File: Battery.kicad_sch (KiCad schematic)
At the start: 12 parts, among them J1 Keystone-1048, J2 Keystone-1048, J3 Keystone-1042, J4 Keystone-1042

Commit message: temporary changes
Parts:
- added D7, D8: BAT60JFILM, Diode_SMD:D_SOD-323_HandSoldering, symbol Device:D_Schottky_Small
- added F12, F13, F14, F15: 5A, Fuse:Fuse_1206_3216Metric, symbol Device:Fuse_Small
- added J11: (no value), Argus-Battery:21700_battery_holder_th, symbol Argus-Battery:21700_batt_holder_th
- D1, D2, F1, F2, F3, F4, F5, F6, J1, J2, J3, J4: now not fitted
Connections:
- net BATT_M: now also D7.1 (K), D8.2 (A), J11.5 (neg1), J11.6 (neg2), J11.7 (pos3), J11.8 (pos4)
- net BATT_N: now also D7.2 (A), F12.2, F13.2
- net BATT_P: now also D8.1 (K), F14.2, F15.2
- new net: F15.1, J11.2 (pos2)
- new net: F13.1, J11.3 (neg3)
- new net: F12.1, J11.4 (neg4)
- new net: F14.1, J11.1 (pos1)
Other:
- note added: "4x 21700 cells in 2s2p configuration 7.2V nominal, 10000mAh Capacity Molicel 21700 P50B 5000mAh 60A Battery"

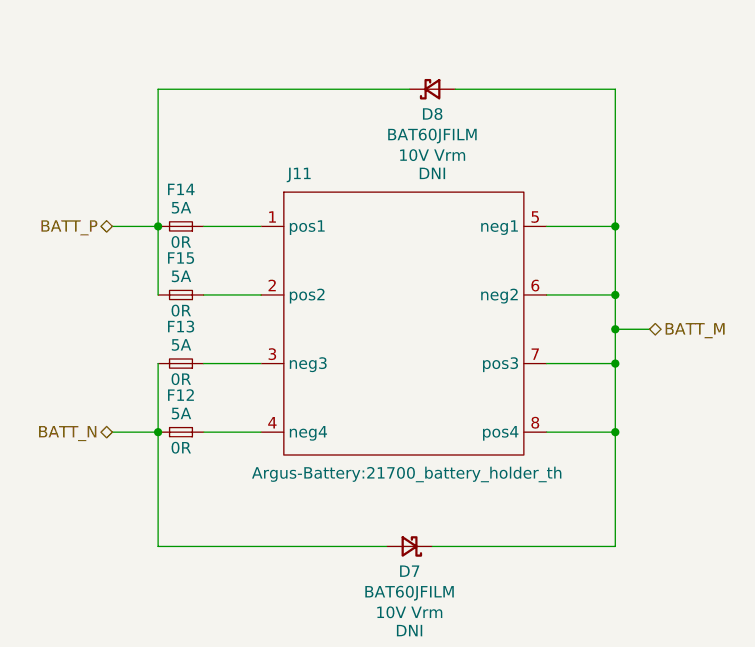
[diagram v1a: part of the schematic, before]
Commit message: placed components start routing
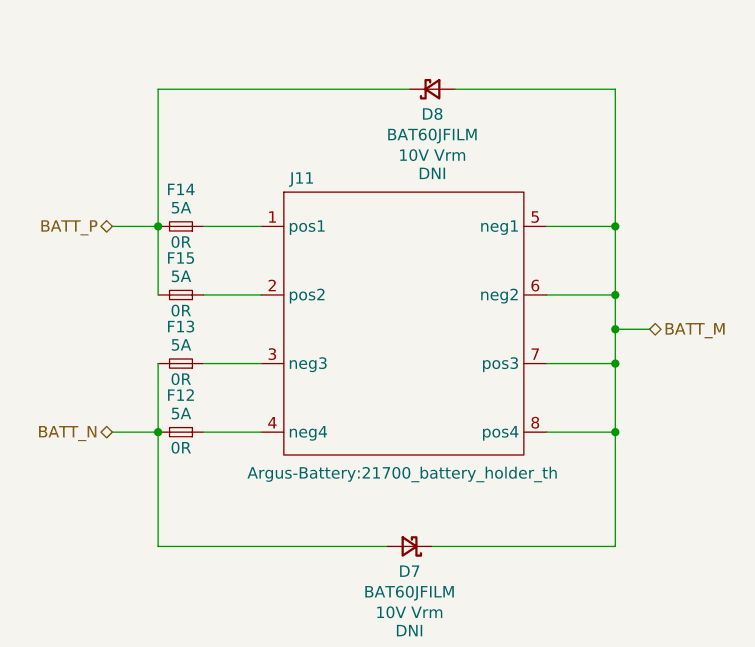
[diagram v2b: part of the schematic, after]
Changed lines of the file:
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@@
+	)
+	(symbol
+		(lib_id "Argus-Battery:21700_batt_holder_th")
+		(at 205.74 64.77 0)
+		(unit 1)
+		(body_style 1)
+		(exclude_from_sim no)
+		(in_bom no)
+		(on_board yes)
+		(in_pos_files no)
+		(dnp no)
+		(property "Reference" "J11"
+			(at 211.582 64.516 0)
+			(show_name no)
+			(do_not_autoplace no)
+			(effects
+				(font
+					(size 1.27 1.27)
+				)
+			)
+		)
+		(property "Value" ""
+			(at 205.74 64.77 0)
+			(show_name no)
+			(do_not_autoplace no)
+			(effects
+				(font
+					(size 1.27 1.27)
+				)
+			)
+		)
+		(property "Footprint" "Argus-Battery:21700_battery_holder_th"
+			(at 222.758 97.282 0)
+			(show_name no)
+			(do_not_autoplace no)
+			(effects
+				(font
+					(size 1.27 1.27)
+				)
+			)
+		)
+		(property "Datasheet" ""
+			(at 205.74 64.77 0)
+			(hide yes)
+			(show_name no)
+			(do_not_autoplace no)
+			(effects
+				(font
+					(size 1.27 1.27)
+				)
+			)
+		)
+		(property "Description" ""
+			(at 205.74 64.77 0)
+			(hide yes)
+			(show_name no)
+			(do_not_autoplace no)
+			(effects
+				(font
+					(size 1.27 1.27)
+				)
+			)
+		)
+		(pin "3"
+		)
+		(pin "1"
+		)
+		(pin "5"
+		)
+		(pin "7"
+		)
+		(pin "6"
+		)
+		(pin "8"
+		)
+		(pin "2"
+		)
+		(pin "4"
+		)
+		(instances
+			(project "Avionics-BatteryBoard"
+				(path "/b6fd875d-6e05-4440-9a05-0f0aa046a0ef/929ad239-5e24-4db1-ba18-c148cf561726"
+					(reference "J11")
+					(unit 1)
+				)
+			)
+		)
 	)
 	(symbol
@@
 					(unit 1)
 				)
-			)
-		)
-	)
-	(symbol
-		(lib_id "Argus-Battery:21700_batt_holder_th")
-		(at 205.74 64.77 0)
-		(unit 1)
-		(body_style 1)
-		(exclude_from_sim no)
-		(in_bom no)
-		(on_board yes)
-		(in_pos_files no)
-		(dnp no)
-		(property "Reference" "J11"
-			(at 211.328 64.008 0)
-			(show_name no)
-			(do_not_autoplace no)
-			(effects
-				(font
-					(size 1.27 1.27)
-				)
-			)
-		)
-		(property "Value" ""
-			(at 205.74 64.77 0)
-			(show_name no)
-			(do_not_autoplace no)
-			(effects
-				(font
-					(size 1.27 1.27)
-				)
-			)
-		)
-		(property "Footprint" "Argus-Battery:21700_battery_holder_th"
-			(at 223.266 97.282 0)
-			(show_name no)
-			(do_not_autoplace no)
-			(effects
-				(font
-					(size 1.27 1.27)
-				)
-			)
-		)
-		(property "Datasheet" ""
-			(at 205.74 64.77 0)
-			(hide yes)
-			(show_name no)
-			(do_not_autoplace no)
-			(effects
-				(font
-					(size 1.27 1.27)
-				)
-			)
-		)
-		(property "Description" ""
-			(at 205.74 64.77 0)
-			(hide yes)
-			(show_name no)
-			(do_not_autoplace no)
-			(effects
-				(font
-					(size 1.27 1.27)
-				)
-			)
-		)
-		(pin "4"
-		)
-		(pin "5"
-		)
-		(pin "6"
-		)
-		(pin "1"
-		)
-		(pin "2"
-		)
-		(pin "3"
-		)
-		(pin "8"
-		)
-		(pin "7"
-		)
-		(instances
-			(project "Avionics-BatteryBoard"
-				(path "/b6fd875d-6e05-4440-9a05-0f0aa046a0ef/929ad239-5e24-4db1-ba18-c148cf561726"
-					(reference "J11")
-					(unit 1)
-				)

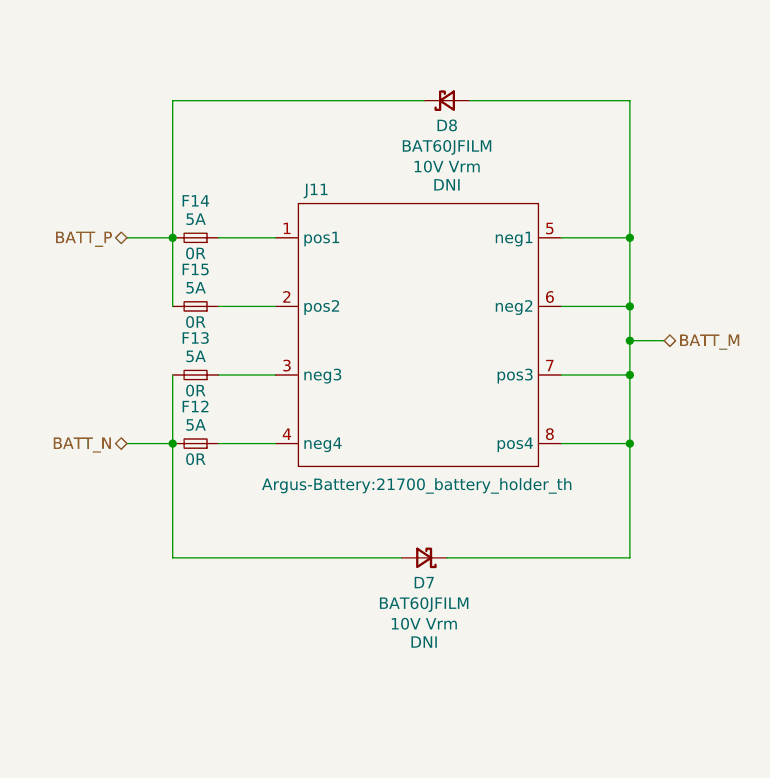
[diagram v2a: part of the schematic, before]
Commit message: batteryboard v4.0 complete, need to fix footprint courtyard so drc passes but othw should be all good
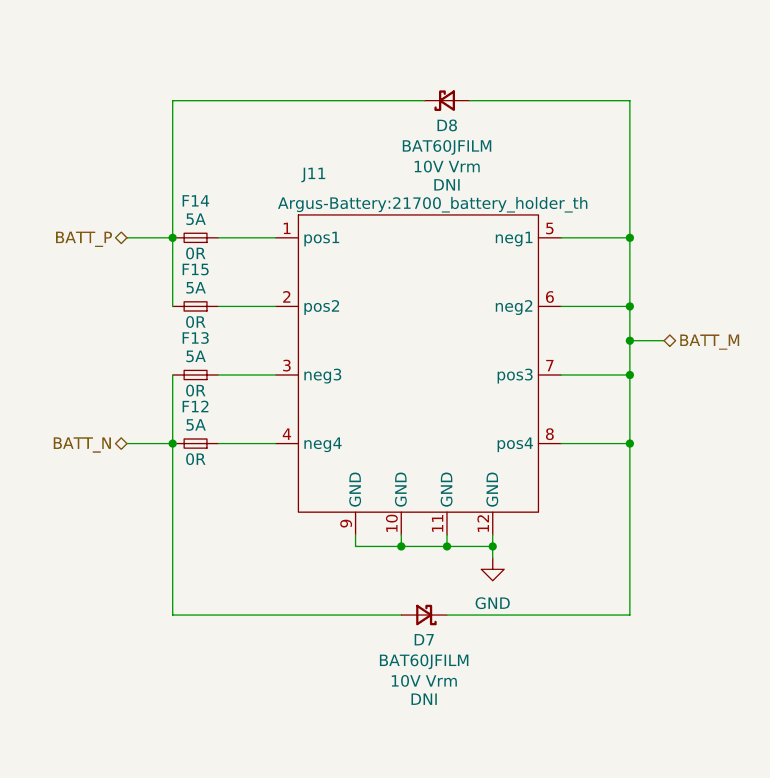
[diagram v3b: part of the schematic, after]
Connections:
- new net GND: J11.10 (GND), J11.11 (GND), J11.12 (GND), J11.9 (GND)
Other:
- moved on the sheet: D7
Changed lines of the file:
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@@
+	)
+	(junction
+		(at 246.38 92.71)
+		(diameter 0)
+		(color 0 0 0 0)
 	)
 	(junction
@@
 	)
 	(junction
+		(at 231.14 104.14)
+		(diameter 0)
+		(color 0 0 0 0)
+	)
+	(junction
 		(at 246.38 69.85)
 		(diameter 0)
@@
 	)
 	(junction
-		(at 246.38 92.71)
+		(at 226.06 104.14)
 		(diameter 0)
 		(color 0 0 0 0)
@@
 	)
 	(junction
+		(at 220.98 104.14)
+		(diameter 0)
+		(color 0 0 0 0)
+	)
+	(junction
 		(at 111.76 101.6)
 		(diameter 0)
@@
 	(wire
 		(pts
+			(xy 215.9 104.14) (xy 220.98 104.14)
+		)
+		(stroke
+			(width 0)
+			(type default)
+		)
+	)
+	(wire
+		(pts
 			(xy 76.2 101.6) (xy 76.2 113.03)
 		)
@@
 	(wire
 		(pts
+			(xy 226.06 104.14) (xy 226.06 102.87)
+		)
+		(stroke
+			(width 0)
+			(type default)
+		)
+	)
+	(wire
+		(pts
 			(xy 200.66 77.47) (xy 207.01 77.47)
 		)
@@
 	(wire
 		(pts
+			(xy 226.06 104.14) (xy 231.14 104.14)
+		)
+		(stroke
+			(width 0)
+			(type default)
+		)
+	)
+	(wire
+		(pts
 			(xy 40.64 90.17) (xy 40.64 101.6)
 		)
@@
 	(wire
 		(pts
+			(xy 220.98 104.14) (xy 220.98 102.87)
+		)
+		(stroke
+			(width 0)
+			(type default)
+		)
+	)
+	(wire
+		(pts
 			(xy 111.76 90.17) (xy 111.76 101.6)
 		)
@@
 	(wire
 		(pts
+			(xy 215.9 104.14) (xy 215.9 102.87)
+		)
+		(stroke
+			(width 0)
+			(type default)
+		)
+	)
+	(wire
+		(pts
 			(xy 107.95 101.6) (xy 111.76 101.6)
 		)
@@
 	(wire
 		(pts
-			(xy 226.06 105.41) (xy 246.38 105.41)
+			(xy 226.06 111.76) (xy 246.38 111.76)
 		)
 		(stroke
@@
 	(wire
 		(pts
+			(xy 220.98 104.14) (xy 226.06 104.14)
+		)
+		(stroke
+			(width 0)
+			(type default)
+		)
+	)
+	(wire
+		(pts
+			(xy 231.14 105.41) (xy 231.14 104.14)
+		)
+		(stroke
+			(width 0)
+			(type default)
+		)
+	)
+	(wire
+		(pts
 			(xy 195.58 54.61) (xy 195.58 69.85)
 		)
@@
 	(wire
 		(pts
-			(xy 246.38 105.41) (xy 246.38 92.71)
+			(xy 231.14 102.87) (xy 231.14 104.14)
+		)
+		(stroke
+			(width 0)
+			(type default)
+		)
+	)
+	(wire
+		(pts
+			(xy 246.38 111.76) (xy 246.38 92.71)
 		)
 		(stroke
@@
 	(wire
 		(pts
-			(xy 195.58 92.71) (xy 195.58 105.41)
+			(xy 195.58 92.71) (xy 195.58 111.76)
 		)
 		(stroke
@@
 	(wire
 		(pts
-			(xy 195.58 105.41) (xy 220.98 105.41)
+			(xy 195.58 111.76) (xy 220.98 111.76)
 		)
 		(stroke
@@
 	(symbol
 		(lib_id "Device:D_Schottky_Small")
-		(at 223.52 105.41 180)
+		(at 223.52 111.76 180)
 		(unit 1)
 		(body_style 1)
@@
 		(dnp no)
 		(property "Reference" "D7"
-			(at 223.52 108.204 0)
+			(at 223.52 114.554 0)
 			(show_name no)
 			(do_not_autoplace no)
@@
 		)
 		(property "Value" "BAT60JFILM"
-			(at 223.52 110.49 0)
+			(at 223.52 116.84 0)
 			(show_name no)
 			(do_not_autoplace no)
@@
 		)
 		(property "Footprint" "Diode_SMD:D_SOD-323_HandSoldering"
-			(at 223.52 105.41 90)
+			(at 223.52 111.76 90)
 			(hide yes)
 			(show_name no)
@@
 		)
 		(property "Datasheet" ""
-			(at 223.52 105.41 90)
+			(at 223.52 111.76 90)
 			(hide yes)
 			(show_name no)
@@
 		)
 		(property "Description" "Schottky diode, small symbol"
-			(at 223.52 105.41 0)
+			(at 223.52 111.76 0)
 			(hide yes)
 			(show_name no)
@@
 		)
 		(property "Field5" "10V Vrm"
-			(at 223.52 112.776 0)
+			(at 223.52 119.126 0)
 			(show_name no)
 			(do_not_autoplace no)
@@
 		)
 		(property "Flight" "DNI"
-			(at 223.52 114.808 0)
+			(at 223.52 121.158 0)
 			(show_name no)
 			(do_not_autoplace no)
@@
 		(dnp no)
 		(property "Reference" "J11"
-			(at 211.582 64.516 0)
+			(at 211.328 62.738 0)
 			(show_name no)
 			(do_not_autoplace no)
@@
 		)
 		(property "Footprint" "Argus-Battery:21700_battery_holder_th"
-			(at 222.758 97.282 0)
+			(at 224.536 66.04 0)
 			(show_name no)
 			(do_not_autoplace no)
@@
 		)
 		(pin "4"
+		)
+		(pin "10"
+		)
+		(pin "12"
+		)
+		(pin "9"
+		)
+		(pin "11"
 		)
 		(instances
@@
 					(unit 1)
 				)
+			)
+		)
+	)
+	(symbol
+		(lib_id "power:GND")
+		(at 231.14 105.41 0)
+		(unit 1)
+		(body_style 1)
+		(exclude_from_sim no)
+		(in_bom yes)
+		(on_board yes)
+		(in_pos_files yes)
+		(dnp no)
+		(fields_autoplaced yes)
+		(property "Reference" "#PWR023"
+			(at 231.14 111.76 0)
+			(hide yes)
+			(show_name no)
+			(do_not_autoplace no)
+			(effects
+				(font
+					(size 1.27 1.27)
+				)
+			)
+		)
+		(property "Value" "GND"
+			(at 231.14 110.49 0)
+			(show_name no)
+			(do_not_autoplace no)
+			(effects
+				(font
+					(size 1.27 1.27)
+				)
+			)
+		)
+		(property "Footprint" ""
+			(at 231.14 105.41 0)
+			(hide yes)
+			(show_name no)
+			(do_not_autoplace no)
+			(effects
+				(font
+					(size 1.27 1.27)
+				)
+			)
+		)
+		(property "Datasheet" ""
+			(at 231.14 105.41 0)
+			(hide yes)
+			(show_name no)
+			(do_not_autoplace no)
+			(effects
+				(font
+					(size 1.27 1.27)
+				)
+			)
+		)
+		(property "Description" "Power symbol creates a global label with name \"GND\" , ground"
+			(at 231.14 105.41 0)
+			(hide yes)
+			(show_name no)
+			(do_not_autoplace no)
+			(effects
+				(font
+					(size 1.27 1.27)
+				)
+			)
+		)
+		(pin "1"
+		)
+		(instances
+			(project "Avionics-BatteryBoard"
+				(path "/b6fd875d-6e05-4440-9a05-0f0aa046a0ef/929ad239-5e24-4db1-ba18-c148cf561726"
+					(reference "#PWR023")
+					(unit 1)
+				)

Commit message: making a few changes
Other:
- title: Argus Batteryboard -> Batteryboard
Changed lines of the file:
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@@
 	(paper "USLetter")
 	(title_block
-		(title "Argus Batteryboard")
-		(date "2026-04-14")
-		(rev "v3.2")
+		(title "Batteryboard")
+		(date "2026-08-21")
+		(rev "v4.0")
 		(company "Carnegie Mellon University")
-		(comment 1 "M. Holliday")
-		(comment 2 "N. Khera")
-		(comment 3 "V. Rajesh")
+		(comment 1 "N. Khera")
+		(comment 2 "V. Rajesh")
+		(comment 3 "S. Farhan")
 	)
 	(rectangle

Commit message: routing
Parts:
- removed D1, D2: BAT60JFILM, Diode_SMD:D_SOD-323_HandSoldering, symbol Device:D_Schottky_Small
- removed F1, F2, F3, F4, F5, F6: 5A, Fuse:Fuse_1206_3216Metric, symbol Device:Fuse_Small
- removed J1, J2: Keystone-1048, Argus-Misc:BAT_1048, symbol Argus-Misc:Keystone-1048
- removed J3, J4: Keystone-1042, Argus-Misc:Keystone_1042, symbol Argus-Misc:Keystone-1042
- J1: renamed from J11; value (none) -> 21700 Holder
- renumbered D7 to D1, D8 to D2, F13 to F1, F12 to F2, F15 to F3, F14 to F4
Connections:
- net BATT_P: now also F3.1, F4.1; no longer F3.2, F4.2
- net at J1.1 (POS): now also F4.2; no longer F4.1
- net at J1.2 (POS): now also F3.2; no longer F3.1
- net at J1.3 (NEG): now also F2.1; no longer F1.1
- net at J1.4 (NEG): now also F1.1; no longer F2.1
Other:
- note removed: "6x 18650 cells in 2S3P arrangement Panasonic NCR18650GA. 3450mAh. 10350mAh total Samsung 35E. 3500mAh = 10500mAh total 7.2V nominal, 8.4V max"
- moved on the sheet: D1, D2, F1, F2, F3, F4
